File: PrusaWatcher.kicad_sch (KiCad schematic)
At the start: 3 parts, among them J1 Raspberry_Pi_2_3, U1 LM2596T-5

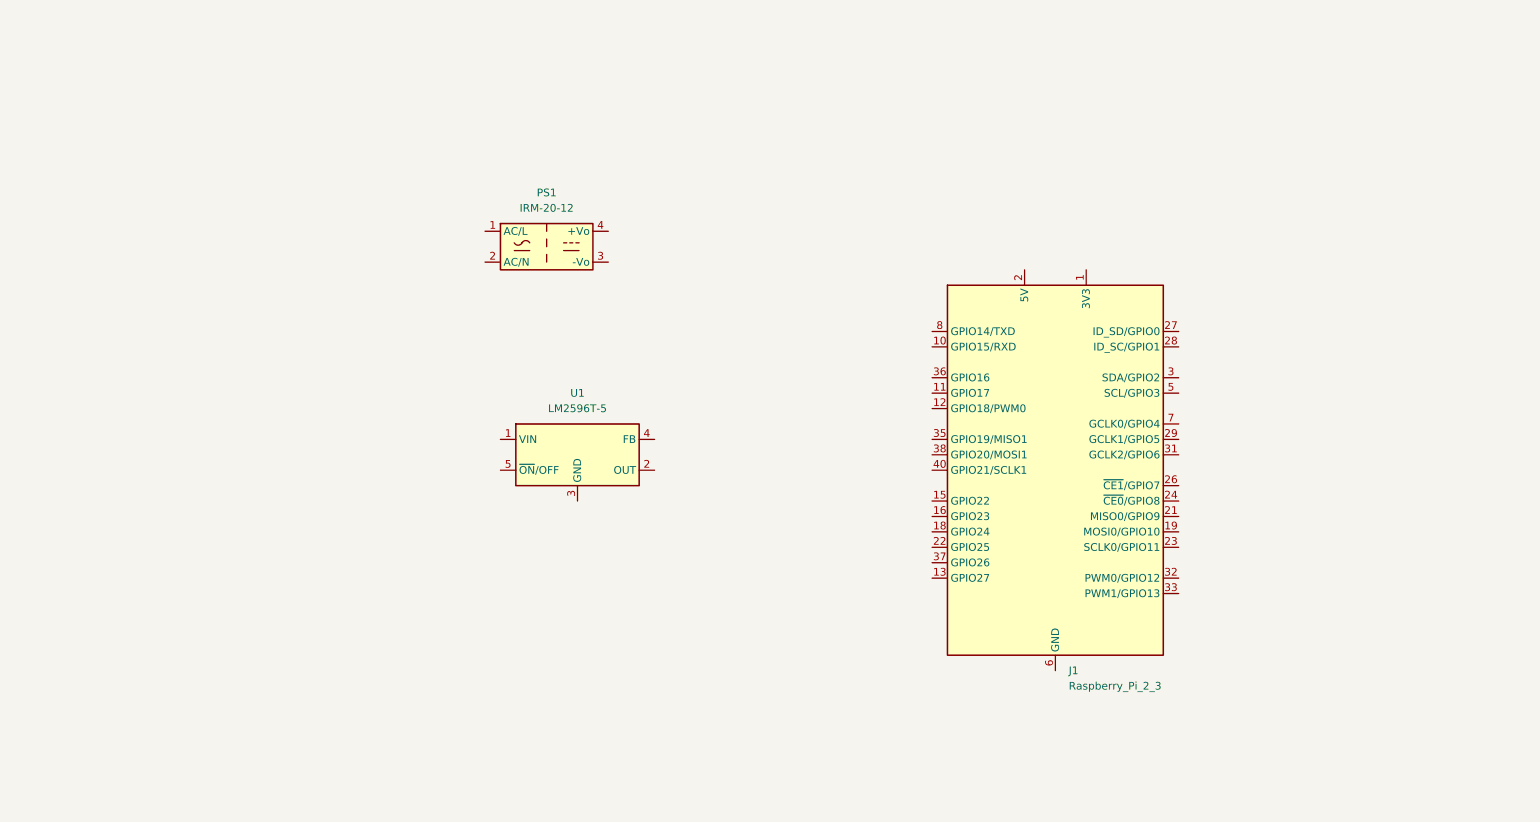
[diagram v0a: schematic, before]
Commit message: Add converter valeus for LM2596
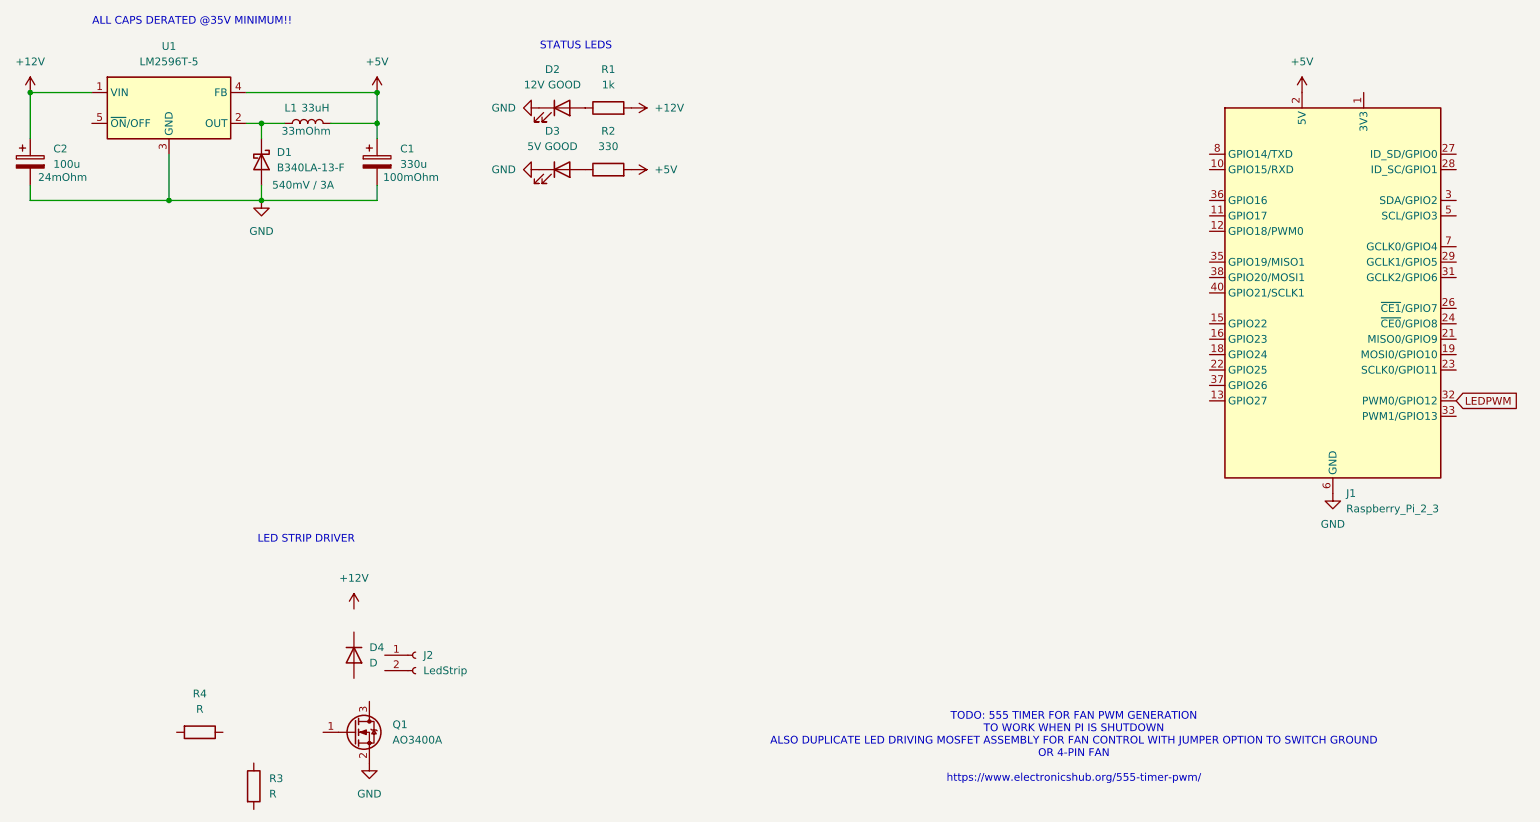
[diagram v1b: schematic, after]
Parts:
- removed PS1: IRM-20-12, Converter_ACDC:Converter_ACDC_MeanWell_IRM-20-xx_THT, symbol Converter_ACDC:IRM-20-12
- added C1: 330u, symbol Device:C_Polarized
- added C2: 100u, symbol Device:C_Polarized
- added D1: B340LA-13-F, symbol Device:D_Schottky
- added D2: 12V GOOD, symbol Device:LED
- added D3: 5V GOOD, symbol Device:LED
- added D4: D, symbol Device:D
- added J2: LedStrip, symbol Connector:Conn_01x02_Socket
- added L1: 33uH, symbol Device:L
- added Q1: AO3400A, Package_TO_SOT_SMD:SOT-23, symbol Transistor_FET:AO3400A
- added R1: 1k, symbol Device:R
- added R2: 330, symbol Device:R
- added R3, R4: R, symbol Device:R
- U1: Link (none) -> https://www.tme.eu/ro/details/lm2596r-5.0-tt/regulatoare-de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
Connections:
- net GND: now reaches J1.14 (GND), J1.20 (GND), J1.25 (GND), J1.30 (GND), J1.34 (GND), J1.39 (GND), J1.6 (GND), J1.9 (GND)
- net GND: now also U1.3 (GND), C1.2, C2.2, D1.2 (A), D2.1 (K), D3.1 (K), Q1.2 (S)
- net +5V: now reaches J1.2 (5V), J1.4 (5V)
- net +5V: now also U1.4 (FB), C1.1, L1.2, R2.2
- net LEDPWM: now reaches J1.32 (PWM0/GPIO12)
- net +12V: now reaches U1.1 (VIN)
- net +12V: now also C2.1, R1.2
- net at U1.2 (OUT): now also D1.1 (K), L1.1
- new net: D2.2 (A), R1.1
- new net: D3.2 (A), R2.1
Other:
- note added: "ALL CAPS DERATED @35V MINIMUM!!"
- note added: "LED STRIP DRIVER"
- note added: "STATUS LEDS"
- note added: "TODO: 555 TIMER FOR FAN PWM GENERATION TO WORK WHEN PI IS SHUTDOWN ALSO DUPLICATE LED DRIVING MOSFET ASSEMBLY FOR FAN CONTROL WITH JUMPER OPTION TO SWITCH GROUND OR 4-PIN FAN https://www.electronicshub.org/555-timer-pwm/"
- moved on the sheet: J1, U1
